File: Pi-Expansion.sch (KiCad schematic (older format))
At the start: 12 parts, among them J1 RPi_GPIO, J2 SMA_H, P1 BATT, Q1 IRLML6344TRPBF, U1 A2200-A, U2 SPX2920U-5.0

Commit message: did a full layout of the pcb, should be pretty much compleat, also fixed yet more issues librarys
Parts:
- removed Q1: IRLML6344TRPBF, FT:SOT23_FET, symbol MOSFET_N
- added D1: D, Diodes_ThroughHole:Diode_DO-41_SOD81_Horizontal_RM10, symbol D
- added F1: FUSE, Fuse_Holders_and_Fuses:Fuse_SMD1206_HandSoldering, symbol FUSE
- LED1, LED2, LED3, LED4: symbol LED -> LED-RESCUE-Pi-Expansion
- R1, R2: symbol R -> R-RESCUE-Pi-Expansion
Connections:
- net labels added: GPS_WAKE
- net labels removed: GPS_ON_OFF, GPS_RESET, GPS_WAKEUP
- wire segments 53 -> 47
- no-connect marks 0 -> 37
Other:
- moved on the sheet: P1
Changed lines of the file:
@@
 EESchema Schematic File Version 2
-LIBS:freetronics_schematic
+LIBS:Pi-Expansion-rescue
 LIBS:power
 LIBS:device
@@
 LIBS:contrib
 LIBS:valves
-LIBS:Universal
 LIBS:a2200-a
 LIBS:RPi_Hat-cache
+LIBS:freetronics_schematic
+LIBS:Universal
 LIBS:Pi-Expansion-cache
 EELAYER 25 0
@@
 $EndComp
 $Comp
-L LED LED1
+L LED-RESCUE-Pi-Expansion LED1
 U 1 1 56C01A08
 P 9550 5000
@@
 $EndComp
 $Comp
-L LED LED2
+L LED-RESCUE-Pi-Expansion LED2
 U 1 1 56C01AE2
 P 9550 5300
@@
 $EndComp
 $Comp
-L LED LED3
+L LED-RESCUE-Pi-Expansion LED3
 U 1 1 56C01B0C
 P 9550 5600
@@
 $EndComp
 $Comp
-L LED LED4
+L LED-RESCUE-Pi-Expansion LED4
 U 1 1 56C01B3D
 P 9550 5900
@@
 PI_LED_4
 $Comp
-L R R2
+L R-RESCUE-Pi-Expansion R2
 U 1 1 56C02F7F
 P 10350 5450
@@
 Text GLabel 3750 5500 2    55   Input ~ 0
 GPS_RX
-Text GLabel 1250 5500 0    55   Input ~ 0
+Text GLabel 3650 6700 2    55   Input ~ 0
 PI_LED_1
-Text GLabel 1250 5700 0    55   Input ~ 0
+Text GLabel 3650 6900 2    55   Input ~ 0
 PI_LED_2
-Text GLabel 1250 5800 0    55   Input ~ 0
+Text GLabel 3650 7000 2    55   Input ~ 0
 PI_LED_3
-Text GLabel 1250 5900 0    55   Input ~ 0
+Text GLabel 3650 7100 2    55   Input ~ 0
 PI_LED_4
 $Comp
@@
 	1    0    0    -1
 $EndComp
-Text GLabel 2250 1500 0    60   Input ~ 0
-GPS_ON_OFF
-$Comp
-L R R1
+$Comp
+L R-RESCUE-Pi-Expansion R1
 U 1 1 56C04659
 P 5650 2600
@@
 Connection ~ 10100 5600
 Wire Wire Line
-	1350 7250 1350 7100
+	1350 7100 1350 7250
 Wire Wire Line
 	1350 7100 1500 7100
@@
 	3400 5600 3750 5600
 Wire Wire Line
-	1250 5800 1500 5800
-Wire Wire Line
-	1250 5900 1500 5900
+	3650 7000 3400 7000
+Wire Wire Line
+	3650 7100 3400 7100
 Wire Wire Line
 	2250 2100 2400 2100
@@
 	2100 2700 2400 2700
 Wire Wire Line
-	2250 1500 2400 1500
-Wire Wire Line
 	4250 1500 5650 1500
 Wire Wire Line
@@
 Wire Wire Line
 	5650 3300 5650 2850
-Text GLabel 2250 1700 0    60   Input ~ 0
-GPS_WAKEUP
-Wire Wire Line
-	2400 1700 2250 1700
-Text GLabel 2250 1900 0    60   Input ~ 0
-GPS_RESET
-Wire Wire Line
-	2400 1900 2250 1900
 Text Notes 4300 3450 0    60   ~ 0
 SPI PINS
-Text GLabel 3750 5700 2    55   Input ~ 0
-GPS_ON_OFF
-Wire Wire Line
-	3400 5700 3750 5700
-Text GLabel 3750 5900 2    55   Input ~ 0
-GPS_WAKEUP
-Wire Wire Line
-	3400 5900 3750 5900
-Text GLabel 3750 6000 2    55   Input ~ 0
-GPS_RESET
-Wire Wire Line
-	3400 6000 3750 6000
-Wire Wire Line
-	1250 5700 1500 5700
-Wire Wire Line
-	1250 5500 1500 5500
-$Comp
-L MOSFET_N Q1
-U 1 1 56C071B7
-P 9500 1150
-F 0 "Q1" V 9410 1320 60  0000 R CNN
-F 1 "IRLML6344TRPBF" V 9560 900 60  0000 R CNN
-F 2 "FT:SOT23_FET" H 9500 1150 60  0001 C CNN
-F 3 "" H 9500 1150 60  0000 C CNN
-	1    9500 1150
-	0    1    1    0
-$EndComp
-Wire Wire Line
-	9300 1250 9250 1250
+Wire Wire Line
+	3650 6900 3400 6900
+Wire Wire Line
+	3650 6700 3400 6700
 $Comp
 L SPX2920U-5.0 U2
@@
 $EndComp
 Wire Wire Line
-	9050 900  10000 900
-Connection ~ 9500 900
-Wire Wire Line
-	9700 1250 10950 1250
-Wire Wire Line
 	10400 1250 10400 1200
 $Comp
 L CONN_01X02 P1
 U 1 1 56C07B0C
-P 9000 700
-F 0 "P1" H 9000 850 50  0000 C CNN
-F 1 "BATT" V 9100 700 50  0000 C CNN
-F 2 "Sockets_MOLEX_KK-System:Socket_MOLEX-KK-RM2-54mm_Lock_2pin_straight" H 9000 700 50  0001 C CNN
-F 3 "" H 9000 700 50  0000 C CNN
-	1    9000 700
+P 8650 700
+F 0 "P1" H 8650 850 50  0000 C CNN
+F 1 "BATT" V 8750 700 50  0000 C CNN
+F 2 "Sockets_MOLEX_KK-System:Socket_MOLEX-KK-RM2-54mm_Lock_2pin_straight" H 8650 700 50  0001 C CNN
+F 3 "" H 8650 700 50  0000 C CNN
+	1    8650 700
 	0    -1   -1   0
 $EndComp
-Wire Wire Line
-	9250 1250 9250 1100
-Wire Wire Line
-	9250 1100 8950 1100
-Wire Wire Line
-	8950 1100 8950 900
-Wire Wire Line
-	9500 950  9500 900
 $Comp
 L +5V #PWR06
@@
 Wire Wire Line
 	3400 5200 3650 5200
-Wire Wire Line
-	3400 5300 3650 5300
-Wire Wire Line
-	3650 5300 3650 5200
 $Comp
 L +3.3V #PWR08
@@
 Wire Wire Line
 	4700 2100 4250 2100
+$Comp
+L FUSE F1
+U 1 1 56C2331F
+P 9100 900
+F 0 "F1" H 9200 950 50  0000 C CNN
+F 1 "FUSE" H 9000 850 50  0000 C CNN
+F 2 "Fuse_Holders_and_Fuses:Fuse_SMD1206_HandSoldering" H 9100 900 50  0001 C CNN
+F 3 "" H 9100 900 50  0000 C CNN
+	1    9100 900
+	1    0    0    -1
+$EndComp
+Wire Wire Line
+	9350 900  10000 900
+Wire Wire Line
+	8700 900  8850 900
+Wire Wire Line
+	9250 1250 10950 1250
+Wire Wire Line
+	8600 1250 8950 1250
+Wire Wire Line
+	8600 1250 8600 900
+$Comp
+L D D1
+U 1 1 56C23E17
+P 9100 1250
+F 0 "D1" H 9100 1350 50  0000 C CNN
+F 1 "D" H 9100 1150 50  0000 C CNN
+F 2 "Diodes_ThroughHole:Diode_DO-41_SOD81_Horizontal_RM10" H 9100 1250 50  0001 C CNN
+F 3 "" H 9100 1250 50  0000 C CNN
+	1    9100 1250
+	1    0    0    -1
+$EndComp
+NoConn ~ 3400 6500
+NoConn ~ 3400 6400
+NoConn ~ 3400 6300
+NoConn ~ 3400 6200
+NoConn ~ 1500 6200
+NoConn ~ 1500 6300
+NoConn ~ 1500 6100
+NoConn ~ 1500 5400
+NoConn ~ 1500 5300
+NoConn ~ 1500 7000
+NoConn ~ 1500 6900
+NoConn ~ 1500 6800
+NoConn ~ 1500 6700
+NoConn ~ 1500 6600
+NoConn ~ 1500 6500
+NoConn ~ 4250 3500
+NoConn ~ 4250 3100
+NoConn ~ 4250 2700
+NoConn ~ 4250 2500
+NoConn ~ 2400 2500
+NoConn ~ 2400 2900
+NoConn ~ 2400 3100
+NoConn ~ 4250 1700
+NoConn ~ 1500 6400
+NoConn ~ 3400 6600
+NoConn ~ 1500 5600
+NoConn ~ 3400 6100
+NoConn ~ 3400 5800
+NoConn ~ 3400 5400
+NoConn ~ 3400 5300
+NoConn ~ 3400 6800
+NoConn ~ 2400 1900
+Text GLabel 3750 5700 2    60   Input ~ 0
+GPS_WAKE
+Wire Wire Line
+	3400 5700 3750 5700
+Text GLabel 2250 1500 0    60   Input ~ 0
+GPS_WAKE
+Wire Wire Line
+	2400 1500 2250 1500
+$Comp
+L GND #PWR010
+U 1 1 56C26D35
+P 2050 1800
+F 0 "#PWR010" H 2050 1550 50  0001 C CNN
+F 1 "GND" H 2050 1650 50  0000 C CNN
+F 2 "" H 2050 1800 50  0000 C CNN
+F 3 "" H 2050 1800 50  0000 C CNN
+	1    2050 1800
+	1    0    0    -1
+$EndComp
+Wire Wire Line
+	2050 1800 2050 1700
+Wire Wire Line
+	2050 1700 2400 1700
+NoConn ~ 1500 5900
+NoConn ~ 1500 5800
+NoConn ~ 1500 5700
+NoConn ~ 1500 5500
+NoConn ~ 1500 6000
 $EndSCHEMATC

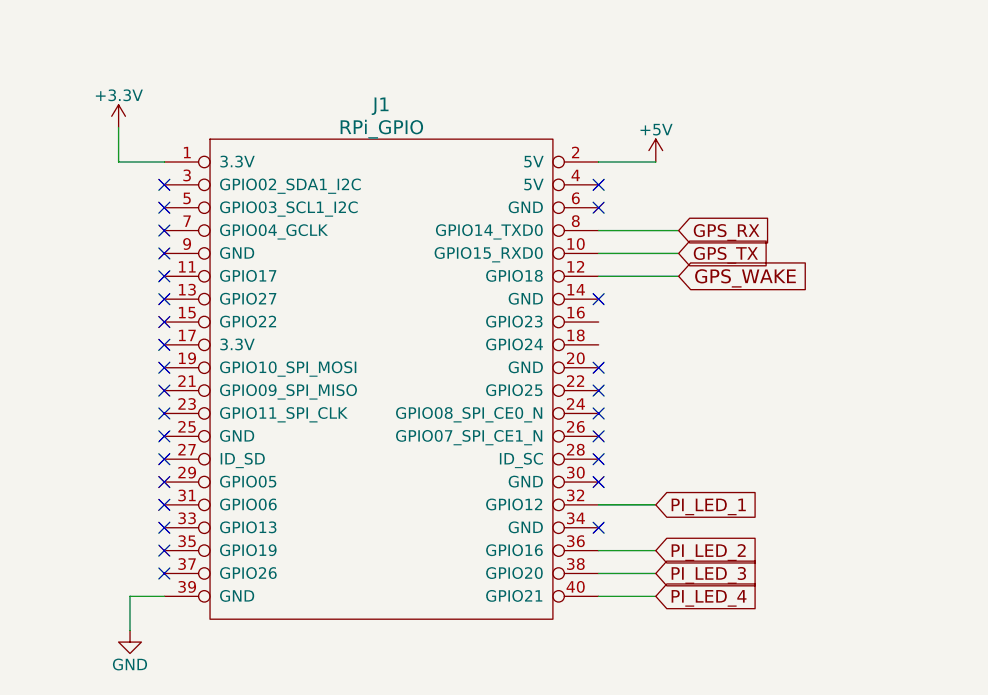
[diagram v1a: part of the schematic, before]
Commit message: Updated 3v3 and Gnd tabs on pi header on schmatic
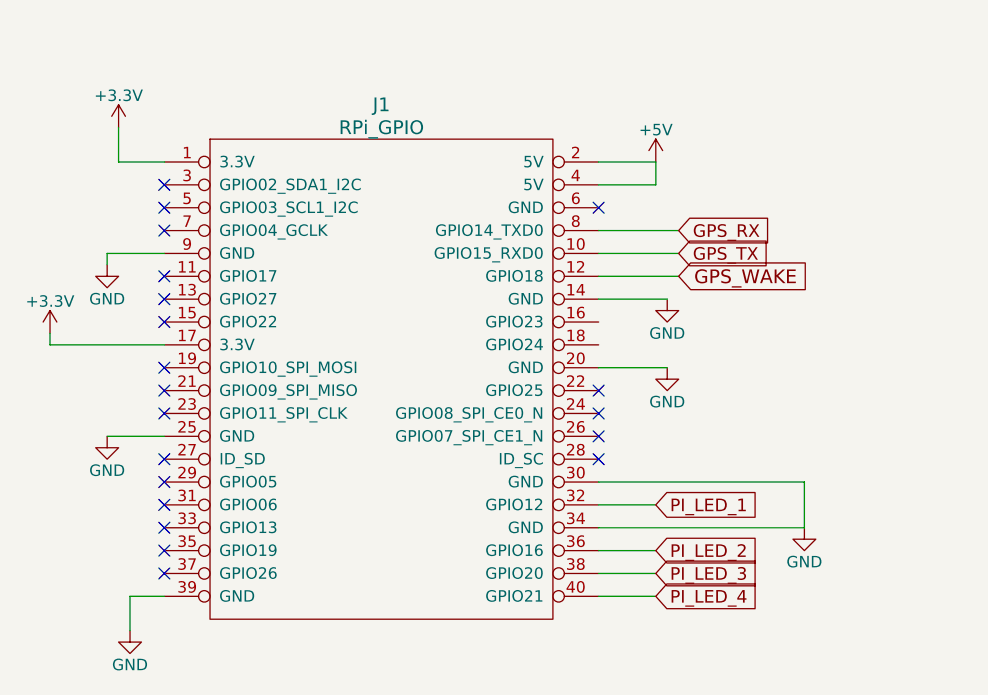
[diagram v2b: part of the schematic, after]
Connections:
- net +3V3: now also J1.17 (3.3V)
- net +5V: now also J1.4 (5V)
- net GND: now also J1.14 (GND), J1.20 (GND), J1.25 (GND), J1.30 (GND), J1.34 (GND), J1.9 (GND)
- no-connect marks 37 -> 29
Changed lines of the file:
@@
 NoConn ~ 2400 3100
 NoConn ~ 4250 1700
-NoConn ~ 1500 6400
-NoConn ~ 3400 6600
-NoConn ~ 1500 5600
-NoConn ~ 3400 6100
-NoConn ~ 3400 5800
 NoConn ~ 3400 5400
-NoConn ~ 3400 5300
-NoConn ~ 3400 6800
 NoConn ~ 2400 1900
 Text GLabel 3750 5700 2    60   Input ~ 0
@@
 NoConn ~ 1500 5700
 NoConn ~ 1500 5500
-NoConn ~ 1500 6000
+$Comp
+L GND #PWR?
+U 1 1 573A1DF2
+P 1250 5650
+F 0 "#PWR?" H 1250 5400 50  0001 C CNN
+F 1 "GND" H 1250 5500 50  0000 C CNN
+F 2 "" H 1250 5650 50  0000 C CNN
+F 3 "" H 1250 5650 50  0000 C CNN
+	1    1250 5650
+	1    0    0    -1
+$EndComp
+$Comp
+L +3.3V #PWR?
+U 1 1 573A1E20
+P 1000 5950
+F 0 "#PWR?" H 1000 5800 50  0001 C CNN
+F 1 "+3.3V" H 1000 6090 50  0000 C CNN
+F 2 "" H 1000 5950 50  0000 C CNN
+F 3 "" H 1000 5950 50  0000 C CNN
+	1    1000 5950
+	1    0    0    -1
+$EndComp
+$Comp
+L GND #PWR?
+U 1 1 573A1E4E
+P 1250 6400
+F 0 "#PWR?" H 1250 6150 50  0001 C CNN
+F 1 "GND" H 1250 6250 50  0000 C CNN
+F 2 "" H 1250 6400 50  0000 C CNN
+F 3 "" H 1250 6400 50  0000 C CNN
+	1    1250 6400
+	1    0    0    -1
+$EndComp
+$Comp
+L GND #PWR?
+U 1 1 573A1E7C
+P 3700 5800
+F 0 "#PWR?" H 3700 5550 50  0001 C CNN
+F 1 "GND" H 3700 5650 50  0000 C CNN
+F 2 "" H 3700 5800 50  0000 C CNN
+F 3 "" H 3700 5800 50  0000 C CNN
+	1    3700 5800
+	1    0    0    -1
+$EndComp
+$Comp
+L GND #PWR?
+U 1 1 573A1EAA
+P 3700 6100
+F 0 "#PWR?" H 3700 5850 50  0001 C CNN
+F 1 "GND" H 3700 5950 50  0000 C CNN
+F 2 "" H 3700 6100 50  0000 C CNN
+F 3 "" H 3700 6100 50  0000 C CNN
+	1    3700 6100
+	1    0    0    -1
+$EndComp
+$Comp
+L GND #PWR?
+U 1 1 573A1ED8
+P 4300 6800
+F 0 "#PWR?" H 4300 6550 50  0001 C CNN
+F 1 "GND" H 4300 6650 50  0000 C CNN
+F 2 "" H 4300 6800 50  0000 C CNN
+F 3 "" H 4300 6800 50  0000 C CNN
+	1    4300 6800
+	1    0    0    -1
+$EndComp
+Wire Wire Line
+	3400 5800 3700 5800
+Wire Wire Line
+	3400 6100 3700 6100
+Wire Wire Line
+	3400 6600 4300 6600
+Wire Wire Line
+	4300 6600 4300 6800
+Wire Wire Line
+	4300 6800 3400 6800
+Wire Wire Line
+	1250 6400 1500 6400
+Wire Wire Line
+	1500 5600 1250 5600
+Wire Wire Line
+	1250 5600 1250 5650
+Wire Wire Line
+	1500 6000 1000 6000
+Wire Wire Line
+	1000 6000 1000 5950
+Wire Wire Line
+	3400 5300 3650 5300
+Wire Wire Line
+	3650 5300 3650 5200
 $EndSCHEMATC

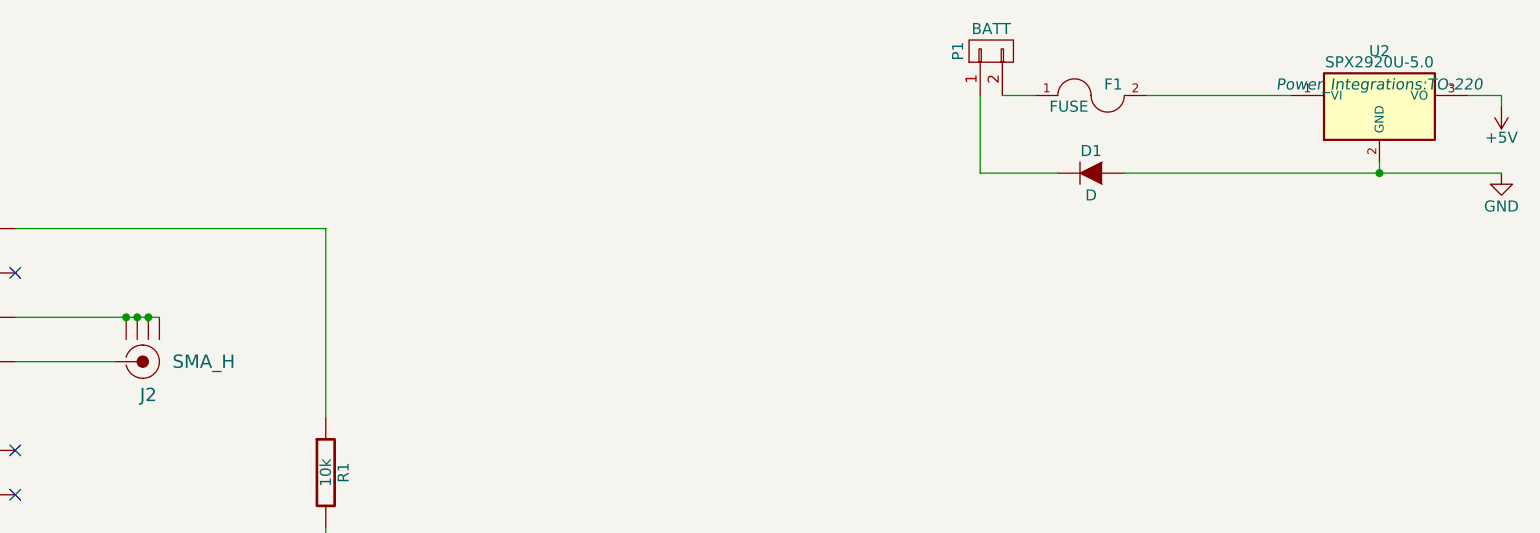
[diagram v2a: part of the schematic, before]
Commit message: Adds reverse voltage protection for DC-DC converter allowing for safe operation of pi form UUSB connector
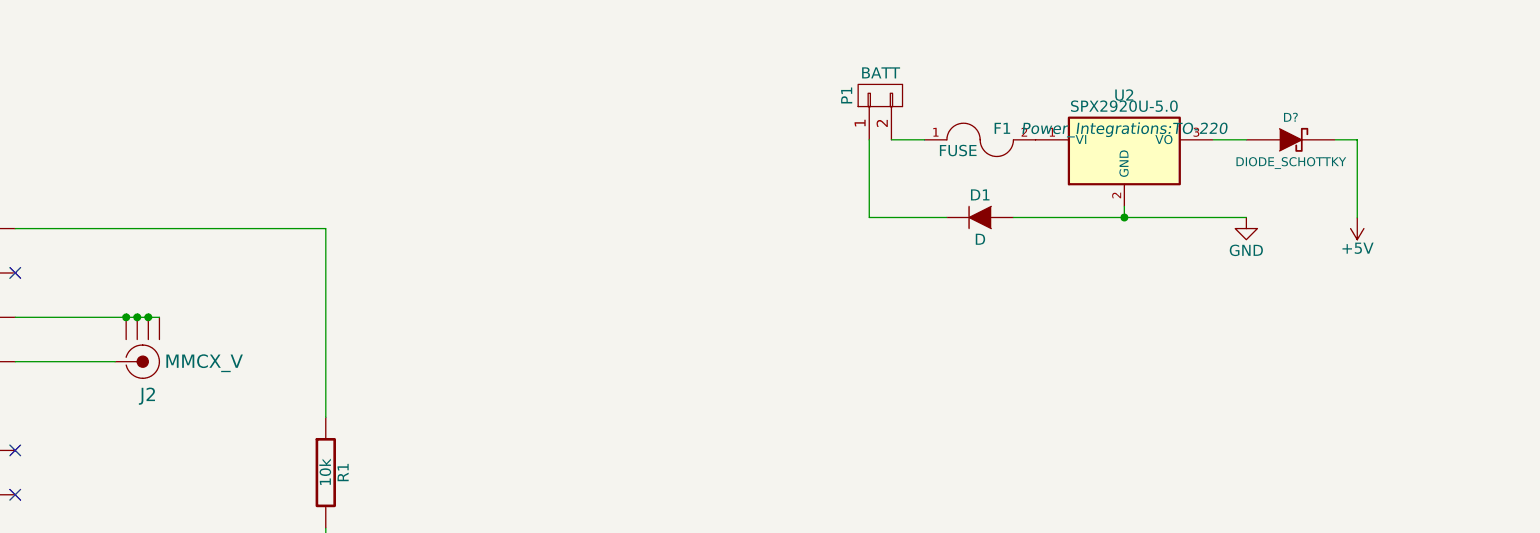
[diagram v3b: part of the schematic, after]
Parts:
- added D?: DIODE_SCHOTTKY, symbol DIODE_SCHOTTKY
- J2: value SMA_H -> MMCX_H; footprint Universal:SMA_H -> Universal:MMCX_V; Component Value SMA_H -> MMCX_V
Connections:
- net +5V: now also D?.K; no longer U2.3 (VO)
- new net: D?.A, U2.3 (VO)
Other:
- moved on the sheet: D1, F1, P1, U2
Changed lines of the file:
@@
 P 4850 1800
 F 0 "J2" H 4850 2250 60  0000 C CNN
-F 1 "SMA_H" H 4750 2400 60  0001 C CNN
-F 2 "Universal:SMA_H" H 4750 2500 60  0001 C CNN
+F 1 "MMCX_H" H 4750 2400 60  0001 C CNN
+F 2 "Universal:MMCX_V" H 4750 2500 60  0001 C CNN
 F 3 "" H 4975 2115 60  0000 C CNN
 F 4 "Digi-Key" H 4750 2950 60  0001 C CNN "Vendor"
@@
 F 7 "142-0711-821" H 4750 2750 60  0001 C CNN "Manufacturer Part Number"
 F 8 "CONN, SMA, JACK, 50 OHM, EDGE MNT," H 4800 2600 60  0001 C CNN "Description"
-F 9 "SMA_H" H 5100 2100 60  0000 C CNN "Component Value"
+F 9 "MMCX_V" H 5100 2100 60  0000 C CNN "Component Value"
 	1    4850 1800
 	1    0    0    1
@@
 L SPX2920U-5.0 U2
 U 1 1 56C0786C
-P 10400 950
-F 0 "U2" H 10400 1200 50  0000 C CNN
-F 1 "SPX2920U-5.0" H 10400 1150 50  0000 C CNN
-F 2 "Power_Integrations:TO-220" H 10400 1050 50  0000 C CIN
-F 3 "" H 10400 950 50  0000 C CNN
-	1    10400 950
-	1    0    0    -1
-$EndComp
-Wire Wire Line
-	10400 1250 10400 1200
+P 9250 1150
+F 0 "U2" H 9250 1400 50  0000 C CNN
+F 1 "SPX2920U-5.0" H 9250 1350 50  0000 C CNN
+F 2 "Power_Integrations:TO-220" H 9250 1250 50  0000 C CIN
+F 3 "" H 9250 1150 50  0000 C CNN
+	1    9250 1150
+	1    0    0    -1
+$EndComp
+Wire Wire Line
+	9250 1450 9250 1400
 $Comp
 L CONN_01X02 P1
 U 1 1 56C07B0C
-P 8650 700
-F 0 "P1" H 8650 850 50  0000 C CNN
-F 1 "BATT" V 8750 700 50  0000 C CNN
-F 2 "Sockets_MOLEX_KK-System:Socket_MOLEX-KK-RM2-54mm_Lock_2pin_straight" H 8650 700 50  0001 C CNN
-F 3 "" H 8650 700 50  0000 C CNN
-	1    8650 700
+P 8150 900
+F 0 "P1" H 8150 1050 50  0000 C CNN
+F 1 "BATT" V 8250 900 50  0000 C CNN
+F 2 "Sockets_MOLEX_KK-System:Socket_MOLEX-KK-RM2-54mm_Lock_2pin_straight" H 8150 900 50  0001 C CNN
+F 3 "" H 8150 900 50  0000 C CNN
+	1    8150 900
 	0    -1   -1   0
 $EndComp
@@
 L +5V #PWR06
 U 1 1 56C07DE9
-P 10950 950
-F 0 "#PWR06" H 10950 800 50  0001 C CNN
-F 1 "+5V" H 10950 1090 50  0000 C CNN
-F 2 "" H 10950 950 50  0000 C CNN
-F 3 "" H 10950 950 50  0000 C CNN
-	1    10950 950
+P 10300 1450
+F 0 "#PWR06" H 10300 1300 50  0001 C CNN
+F 1 "+5V" H 10300 1590 50  0000 C CNN
+F 2 "" H 10300 1450 50  0000 C CNN
+F 3 "" H 10300 1450 50  0000 C CNN
+	1    10300 1450
 	-1   0    0    1
 $EndComp
 Wire Wire Line
-	10800 900  10950 900
-Wire Wire Line
-	10950 900  10950 950
+	9650 1100 9800 1100
+Wire Wire Line
+	10300 1100 10300 1450
 $Comp
 L +5V #PWR07
@@
 L GND #PWR09
 U 1 1 56C08732
-P 10950 1250
-F 0 "#PWR09" H 10950 1000 50  0001 C CNN
-F 1 "GND" H 10950 1100 50  0000 C CNN
-F 2 "" H 10950 1250 50  0000 C CNN
-F 3 "" H 10950 1250 50  0000 C CNN
-	1    10950 1250
-	1    0    0    -1
-$EndComp
-Connection ~ 10400 1250
+P 9800 1450
+F 0 "#PWR09" H 9800 1200 50  0001 C CNN
+F 1 "GND" H 9800 1300 50  0000 C CNN
+F 2 "" H 9800 1450 50  0000 C CNN
+F 3 "" H 9800 1450 50  0000 C CNN
+	1    9800 1450
+	1    0    0    -1
+$EndComp
+Connection ~ 9250 1450
 Wire Wire Line
 	4700 2100 4250 2100
@@
 L FUSE F1
 U 1 1 56C2331F
-P 9100 900
-F 0 "F1" H 9200 950 50  0000 C CNN
-F 1 "FUSE" H 9000 850 50  0000 C CNN
-F 2 "Fuse_Holders_and_Fuses:Fuse_SMD1206_HandSoldering" H 9100 900 50  0001 C CNN
-F 3 "" H 9100 900 50  0000 C CNN
-	1    9100 900
-	1    0    0    -1
-$EndComp
-Wire Wire Line
-	9350 900  10000 900
-Wire Wire Line
-	8700 900  8850 900
-Wire Wire Line
-	9250 1250 10950 1250
-Wire Wire Line
-	8600 1250 8950 1250
-Wire Wire Line
-	8600 1250 8600 900
+P 8600 1100
+F 0 "F1" H 8700 1150 50  0000 C CNN
+F 1 "FUSE" H 8500 1050 50  0000 C CNN
+F 2 "Fuse_Holders_and_Fuses:Fuse_SMD1206_HandSoldering" H 8600 1100 50  0001 C CNN
+F 3 "" H 8600 1100 50  0000 C CNN
+	1    8600 1100
+	1    0    0    -1
+$EndComp
+Wire Wire Line
+	8200 1100 8350 1100
+Wire Wire Line
+	8100 1450 8450 1450
+Wire Wire Line
+	8100 1450 8100 1100
 $Comp
 L D D1
 U 1 1 56C23E17
-P 9100 1250
-F 0 "D1" H 9100 1350 50  0000 C CNN
-F 1 "D" H 9100 1150 50  0000 C CNN
-F 2 "Diodes_ThroughHole:Diode_DO-41_SOD81_Horizontal_RM10" H 9100 1250 50  0001 C CNN
-F 3 "" H 9100 1250 50  0000 C CNN
-	1    9100 1250
+P 8600 1450
+F 0 "D1" H 8600 1550 50  0000 C CNN
+F 1 "D" H 8600 1350 50  0000 C CNN
+F 2 "Diodes_ThroughHole:Diode_DO-41_SOD81_Horizontal_RM10" H 8600 1450 50  0001 C CNN
+F 3 "" H 8600 1450 50  0000 C CNN
+	1    8600 1450
 	1    0    0    -1
 $EndComp
@@
 Wire Wire Line
 	3650 5300 3650 5200
+$Comp
+L DIODE_SCHOTTKY D?
+U 1 1 573A3154
+P 10000 1100
+F 0 "D?" H 10000 1200 40  0000 C CNN
+F 1 "DIODE_SCHOTTKY" H 10000 1000 40  0000 C CNN
+F 2 "" H 10000 1100 60  0000 C CNN
+F 3 "" H 10000 1100 60  0000 C CNN
+	1    10000 1100
+	1    0    0    -1
+$EndComp
+Wire Wire Line
+	10300 1100 10200 1100
+Wire Wire Line
+	8750 1450 9800 1450
 $EndSCHEMATC
